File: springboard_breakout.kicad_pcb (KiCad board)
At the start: 2 copper layers, 47 x 114.3 mm, 3 parts, among them J1 Address & Control Lines, J2 Data Lines, U1 Springboard_Connector

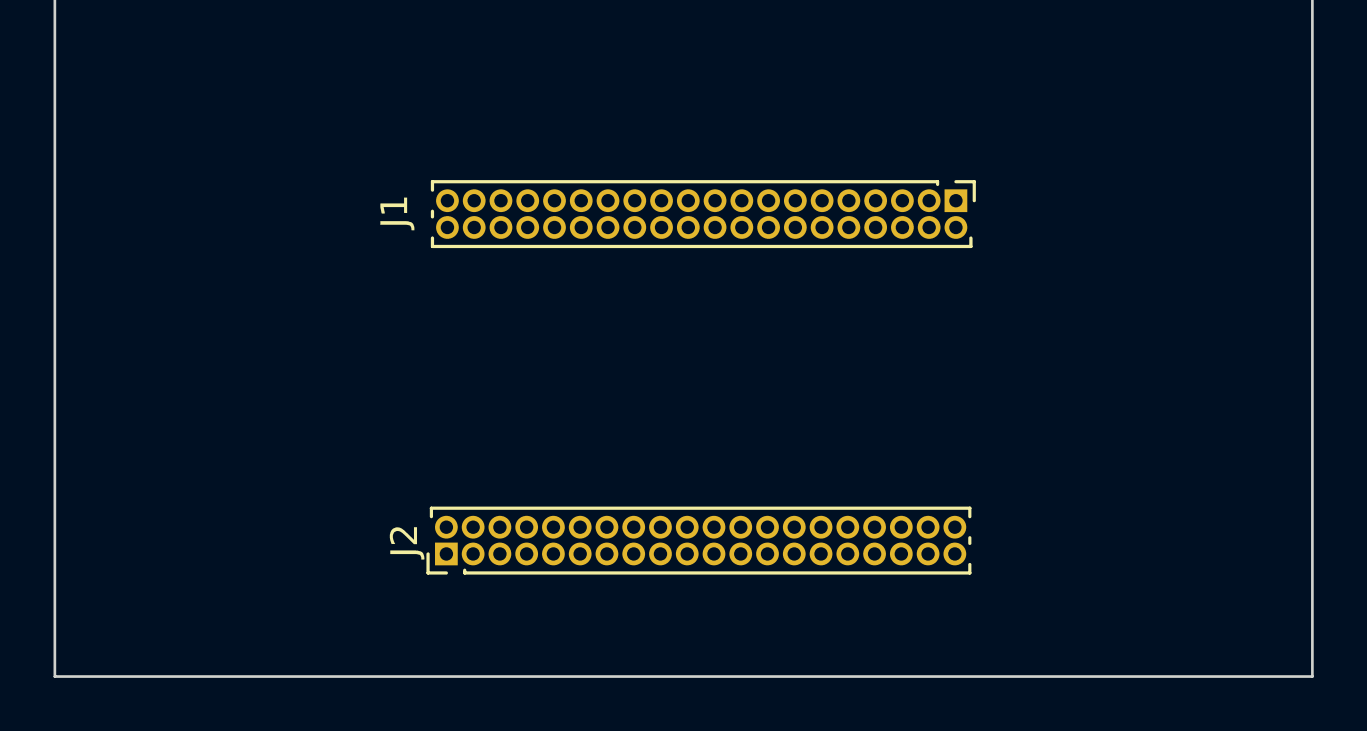
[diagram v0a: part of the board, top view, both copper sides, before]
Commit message: Updated 40 pin header footprint to 2.00 mm pitch
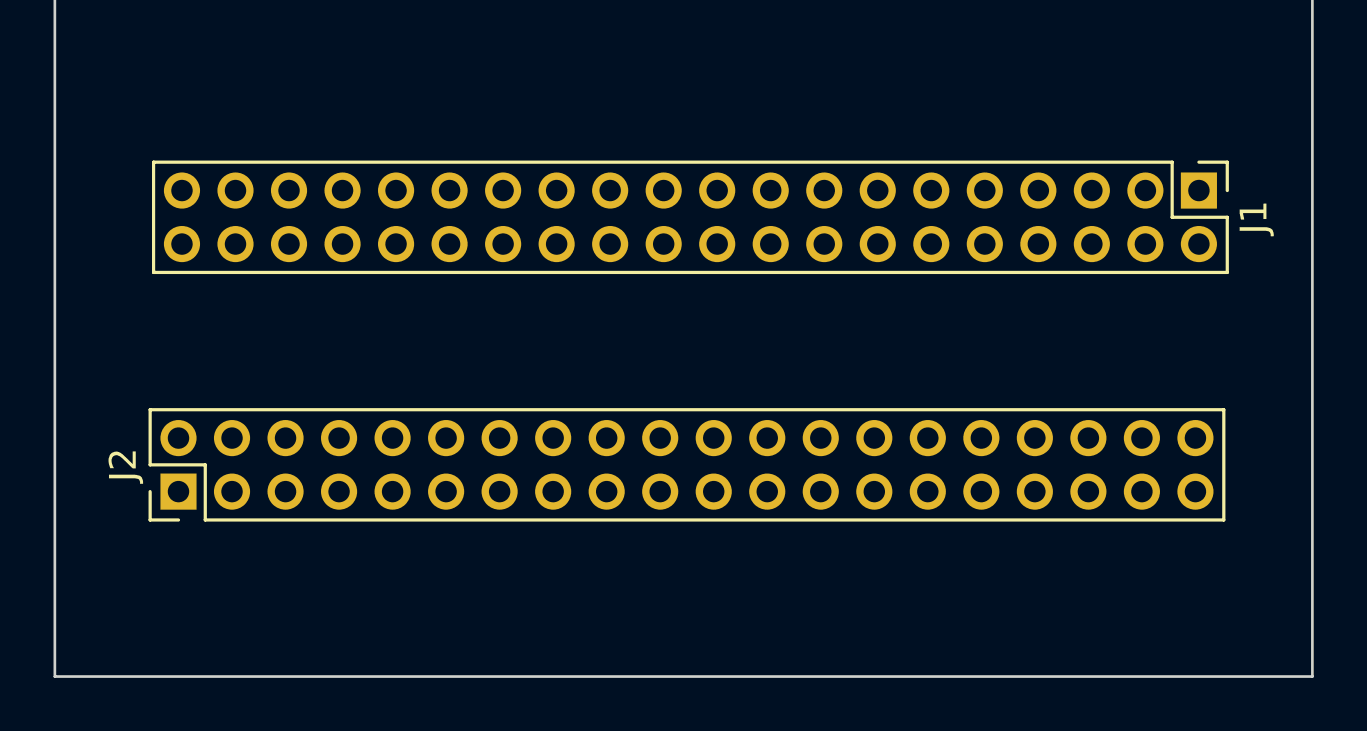
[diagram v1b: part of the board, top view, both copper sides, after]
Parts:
- J1: value Address & Control Lines -> Conn_02x20_Counter_Clockwise; footprint Connector_PinHeader_1.00mm:PinHeader_2x20_P1.00mm_Vertical -> Connector_PinHeader_2.00mm:PinHeader_2x20_P2.00mm_Vertical
- J2: value Data Lines -> Conn_02x20_Counter_Clockwise; footprint Connector_PinHeader_1.00mm:PinHeader_2x20_P1.00mm_Vertical -> Connector_PinHeader_2.00mm:PinHeader_2x20_P2.00mm_Vertical
- moved J2 10.3 mm to (93.5, 145.5)
- moved J1 9.09 mm to (131.7, 134.2)
